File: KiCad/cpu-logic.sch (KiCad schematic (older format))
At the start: 27 parts, among them J1 Barrel_Jack, U1 LM555, U2 74LS05, U3 68000D, X1 CXO_DIP14

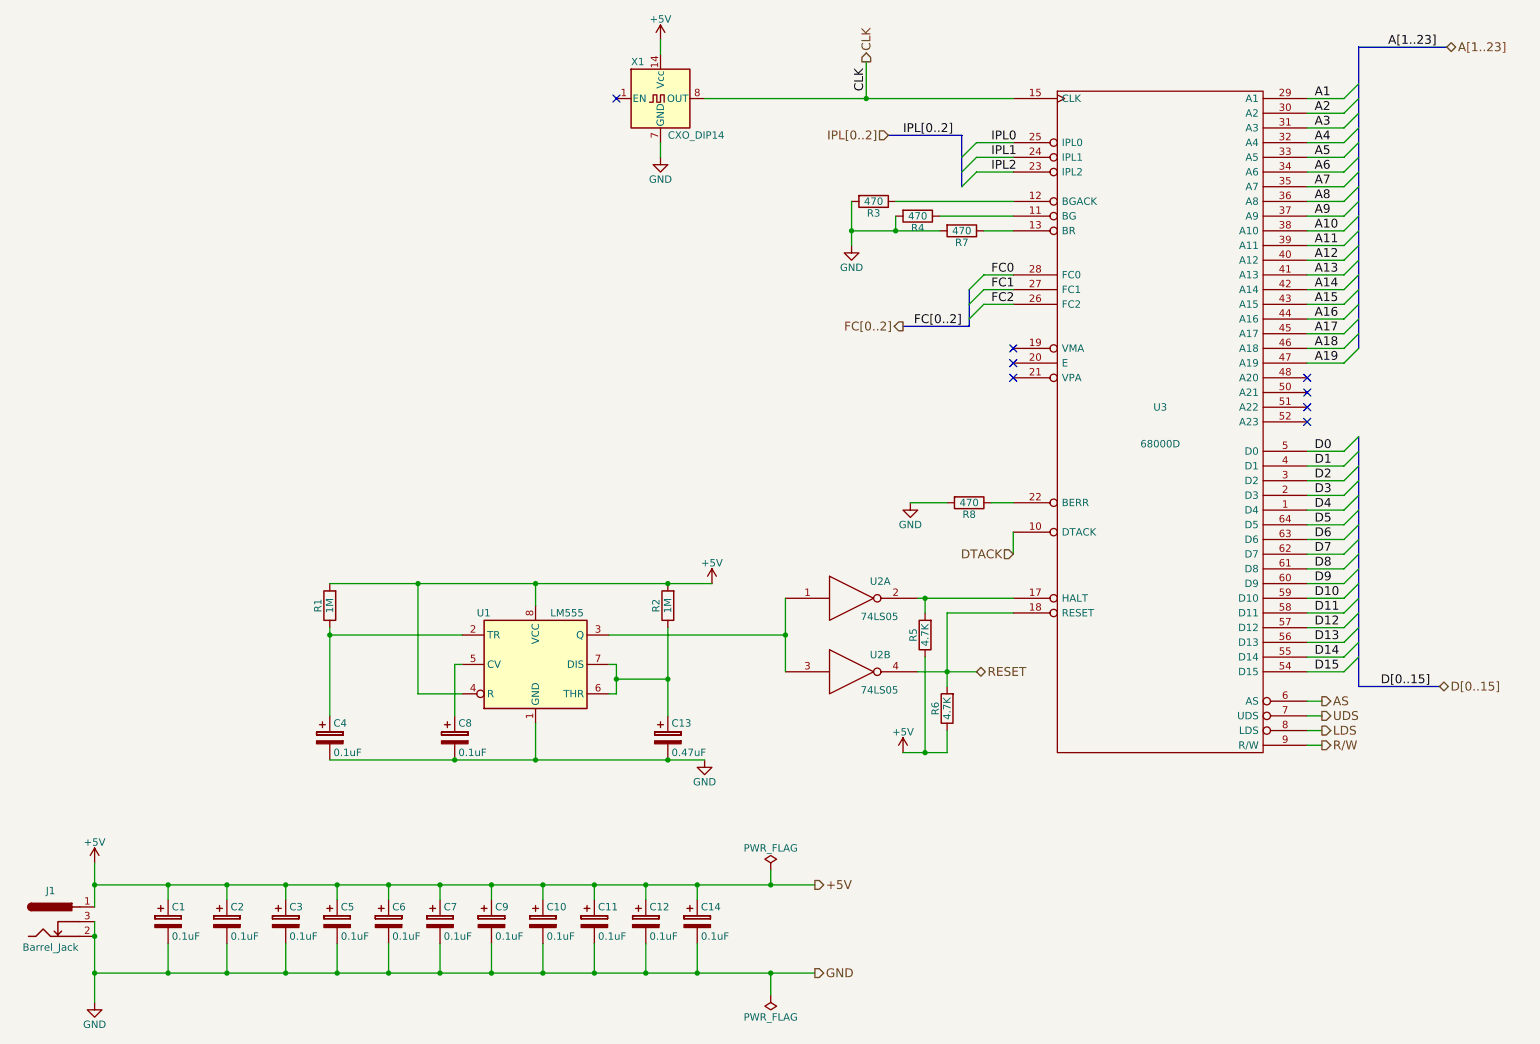
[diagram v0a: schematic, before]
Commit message: begin update for schematic
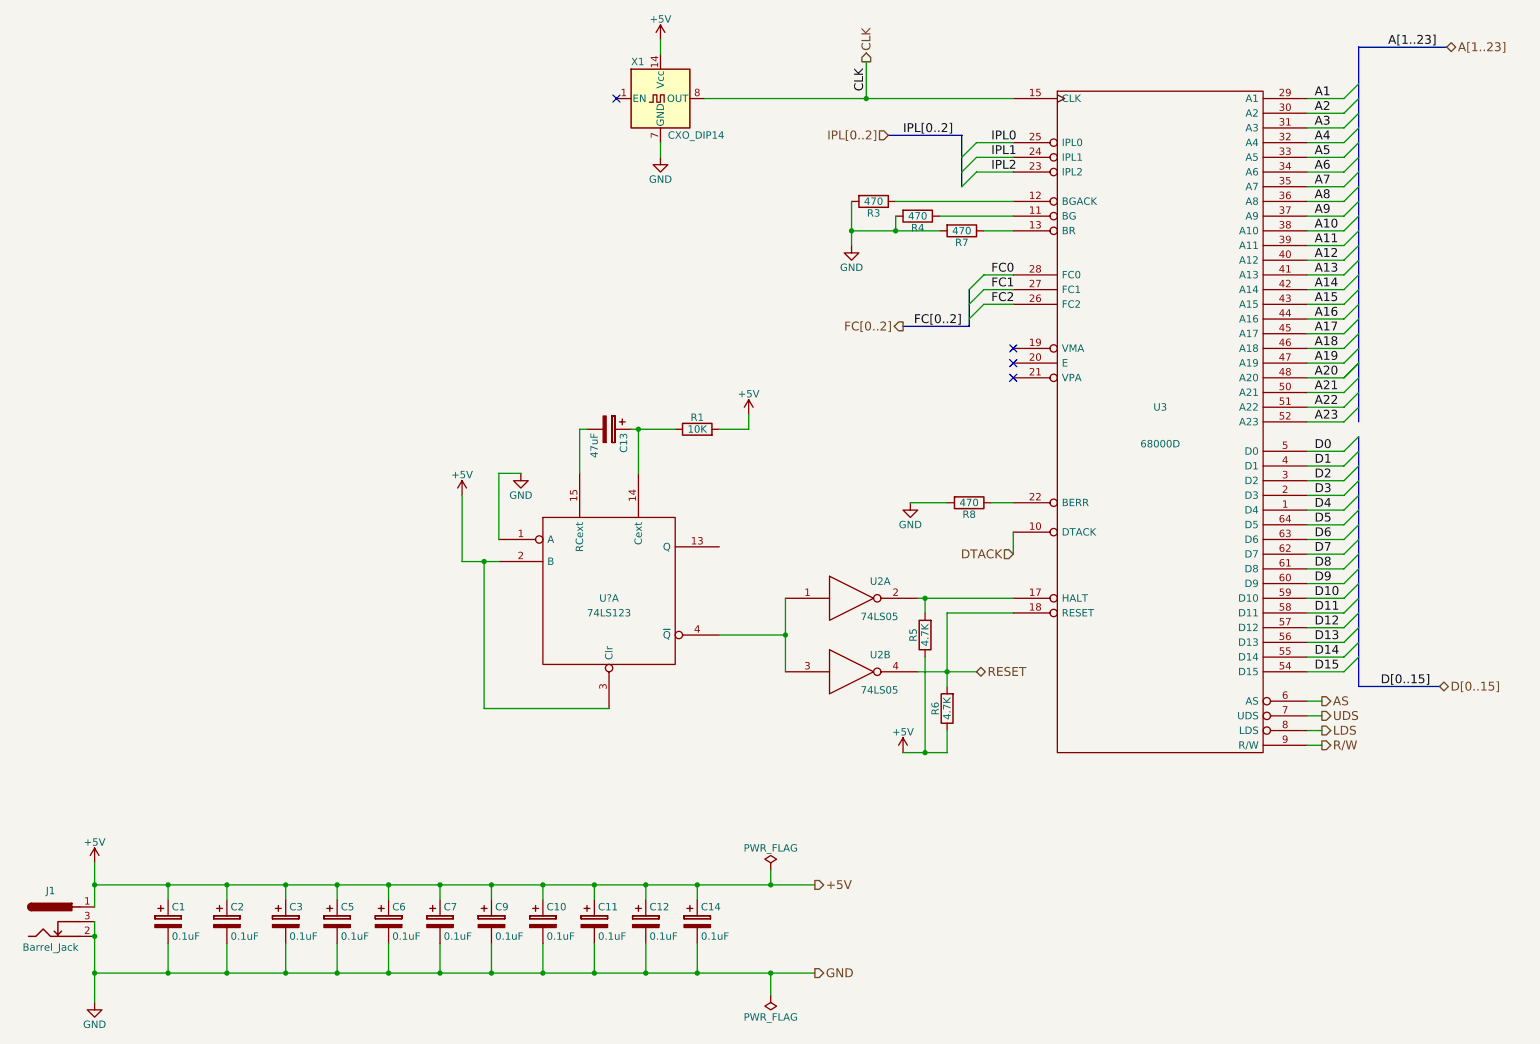
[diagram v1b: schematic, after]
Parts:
- removed C4, C8: 0.1uF, symbol CP
- removed R2: 1M, symbol R
- removed U1: LM555, symbol LM555
- added U?: 74LS123, symbol 74LS123
- C13: value 0.47uF -> 47uF
- R1: value 1M -> 10K
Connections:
- net +5V: now also U?.2 (B), U?.3 (Clr)
- net GND: now also U?.1 (A), U?.8 (GND); no longer C13.2
- net VCC: now also U?.16 (VCC)
- net A20: now reaches U3.48 (A20)
- net A21: now reaches U3.50 (A21)
- net A22: now reaches U3.51 (A22)
- net A23: now reaches U3.52 (A23)
- net at R1.1: now also C13.1, U?.14 (Cext)
- net at U2.1, U2.3: now also U?.4 (~Q)
- new net: C13.2, U?.15 (RCext)
- no-connect marks 8 -> 4
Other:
- moved on the sheet: C13, R1
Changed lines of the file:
@@
 EESchema Schematic File Version 2
 LIBS:Memory_RAM
-LIBS:Oscillator
 LIBS:power
 LIBS:device
@@
 LIBS:valves
 LIBS:Logic_74xx
-LIBS:xc9572xl
-LIBS:Timer_RTC
 LIBS:ds1501y
 LIBS:cp2102
@@
 $EndComp
 $Comp
-L LM555 U1
-U 1 1 5A62B1D1
-P 4250 5250
-F 0 "U1" H 3850 5600 50  0000 L CNN
-F 1 "LM555" H 4350 5600 50  0000 L CNN
-F 2 "" H 4250 5250 50  0001 C CNN
-F 3 "" H 4250 5250 50  0001 C CNN
-	1    4250 5250
-	1    0    0    -1
-$EndComp
-$Comp
 L 74LS05 U2
 U 1 1 5A62B26D
@@
 L +5V #PWR06
 U 1 1 5A62F126
-P 5450 4700
-F 0 "#PWR06" H 5450 4550 50  0001 C CNN
-F 1 "+5V" H 5450 4840 50  0000 C CNN
-F 2 "" H 5450 4700 50  0001 C CNN
-F 3 "" H 5450 4700 50  0001 C CNN
-	1    5450 4700
-	1    0    0    -1
-$EndComp
-$Comp
-L GND #PWR07
-U 1 1 5A62F228
-P 5400 5900
-F 0 "#PWR07" H 5400 5650 50  0001 C CNN
-F 1 "GND" H 5400 5750 50  0000 C CNN
-F 2 "" H 5400 5900 50  0001 C CNN
-F 3 "" H 5400 5900 50  0001 C CNN
-	1    5400 5900
+P 5700 3550
+F 0 "#PWR06" H 5700 3400 50  0001 C CNN
+F 1 "+5V" H 5700 3690 50  0000 C CNN
+F 2 "" H 5700 3550 50  0001 C CNN
+F 3 "" H 5700 3550 50  0001 C CNN
+	1    5700 3550
 	1    0    0    -1
 $EndComp
@@
 L R R1
 U 1 1 5A62F46A
-P 2850 4850
-F 0 "R1" V 2930 4850 50  0000 C CNN
-F 1 "1M" V 2850 4850 50  0000 C CNN
-F 2 "" V 2780 4850 50  0001 C CNN
-F 3 "" H 2850 4850 50  0001 C CNN
-	1    2850 4850
-	-1   0    0    1
-$EndComp
-$Comp
-L CP C8
-U 1 1 5A62F7CA
-P 3700 5750
-F 0 "C8" H 3725 5850 50  0000 L CNN
-F 1 "0.1uF" H 3725 5650 50  0000 L CNN
-F 2 "" H 3738 5600 50  0001 C CNN
-F 3 "" H 3700 5750 50  0001 C CNN
-	1    3700 5750
-	1    0    0    -1
-$EndComp
-$Comp
-L CP C4
-U 1 1 5A63C41B
-P 2850 5750
-F 0 "C4" H 2875 5850 50  0000 L CNN
-F 1 "0.1uF" H 2875 5650 50  0000 L CNN
-F 2 "" H 2888 5600 50  0001 C CNN
-F 3 "" H 2850 5750 50  0001 C CNN
-	1    2850 5750
-	1    0    0    -1
-$EndComp
-$Comp
-L R R2
-U 1 1 5A63C9D1
-P 5150 4850
-F 0 "R2" V 5230 4850 50  0000 C CNN
-F 1 "1M" V 5150 4850 50  0000 C CNN
-F 2 "" V 5080 4850 50  0001 C CNN
-F 3 "" H 5150 4850 50  0001 C CNN
-	1    5150 4850
-	-1   0    0    1
+P 5350 3650
+F 0 "R1" V 5430 3650 50  0000 C CNN
+F 1 "10K" V 5350 3650 50  0000 C CNN
+F 2 "" V 5280 3650 50  0001 C CNN
+F 3 "" H 5350 3650 50  0001 C CNN
+	1    5350 3650
+	0    -1   -1   0
 $EndComp
 $Comp
 L CP C13
 U 1 1 5A63CA8B
-P 5150 5750
-F 0 "C13" H 5175 5850 50  0000 L CNN
-F 1 "0.47uF" H 5175 5650 50  0000 L CNN
-F 2 "" H 5188 5600 50  0001 C CNN
-F 3 "" H 5150 5750 50  0001 C CNN
-	1    5150 5750
-	1    0    0    -1
+P 4750 3650
+F 0 "C13" H 4775 3750 50  0000 L CNN
+F 1 "47uF" H 4775 3550 50  0000 L CNN
+F 2 "" H 4788 3500 50  0001 C CNN
+F 3 "" H 4750 3650 50  0001 C CNN
+	1    4750 3650
+	0    1    1    0
 $EndComp
 $Comp
@@
 	5100 1700 5100 1800
 Wire Wire Line
-	4250 4700 4250 4850
-Wire Wire Line
-	2850 4700 5450 4700
-Wire Wire Line
 	6800 4150 7050 4150
-Connection ~ 4250 4700
-Wire Wire Line
-	3750 5450 3450 5450
-Wire Wire Line
-	3450 5450 3450 4700
-Wire Wire Line
-	4250 5900 4250 5650
-Wire Wire Line
-	2850 5900 5400 5900
-Connection ~ 4250 5900
-Wire Wire Line
-	3700 5600 3700 5250
-Wire Wire Line
-	3700 5250 3750 5250
-Wire Wire Line
-	3750 5050 2850 5050
-Wire Wire Line
-	2850 5000 2850 5600
-Connection ~ 2850 5050
-Connection ~ 3700 5900
-Connection ~ 3450 4700
-Wire Wire Line
-	4750 5250 4800 5250
-Wire Wire Line
-	4800 5250 4800 5450
-Wire Wire Line
-	4800 5450 4750 5450
-Connection ~ 5150 4700
-Wire Wire Line
-	4800 5350 5150 5350
-Wire Wire Line
-	5150 5000 5150 5600
-Connection ~ 4800 5350
-Connection ~ 5150 5350
-Connection ~ 5150 5900
-Wire Wire Line
-	4750 5050 5950 5050
 Wire Wire Line
 	5950 4800 5950 5300
-Connection ~ 5950 5050
 Wire Wire Line
 	6900 5200 6900 5850
@@
 	5350 6850 5350 6750
 Connection ~ 5350 6750
-NoConn ~ 9500 3300
-NoConn ~ 9500 3400
-NoConn ~ 9500 3500
-NoConn ~ 9500 3600
 Wire Bus Line
-	9850 1050 9850 3100
+	9850 1050 9850 3600
+$Comp
+L 74LS123 U?
+U 1 1 5B522F26
+P 4750 4750
+F 0 "U?" H 4750 4700 50  0000 C CNN
+F 1 "74LS123" H 4750 4600 50  0000 C CNN
+F 2 "" H 4750 4750 50  0001 C CNN
+F 3 "" H 4750 4750 50  0001 C CNN
+	1    4750 4750
+	1    0    0    -1
+$EndComp
+Wire Wire Line
+	4550 3950 4550 3650
+Wire Wire Line
+	4550 3650 4600 3650
+Wire Wire Line
+	4950 3950 4950 3650
+Wire Wire Line
+	4900 3650 5200 3650
+Connection ~ 4950 3650
+Wire Wire Line
+	5500 3650 5700 3650
+Wire Wire Line
+	5700 3650 5700 3550
+$Comp
+L GND #PWR?
+U 1 1 5B524750
+P 4150 3950
+F 0 "#PWR?" H 4150 3700 50  0001 C CNN
+F 1 "GND" H 4150 3800 50  0000 C CNN
+F 2 "" H 4150 3950 50  0001 C CNN
+F 3 "" H 4150 3950 50  0001 C CNN
+	1    4150 3950
+	1    0    0    -1
+$EndComp
+$Comp
+L +5V #PWR?
+U 1 1 5B5247BB
+P 3750 4100
+F 0 "#PWR?" H 3750 3950 50  0001 C CNN
+F 1 "+5V" H 3750 4240 50  0000 C CNN
+F 2 "" H 3750 4100 50  0001 C CNN
+F 3 "" H 3750 4100 50  0001 C CNN
+	1    3750 4100
+	1    0    0    -1
+$EndComp
+Wire Wire Line
+	4000 4550 3750 4550
+Wire Wire Line
+	3750 4550 3750 4100
+Wire Wire Line
+	4150 3950 4000 3950
+Wire Wire Line
+	4000 3950 4000 4400
+Wire Wire Line
+	4750 5550 3900 5550
+Wire Wire Line
+	3900 5550 3900 4550
+Connection ~ 3900 4550
+Wire Wire Line
+	5500 5050 5950 5050
+Connection ~ 5950 5050
+Wire Wire Line
+	9500 3300 9750 3300
+Wire Wire Line
+	9500 3400 9750 3400
+Wire Wire Line
+	9500 3500 9750 3500
+Wire Wire Line
+	9500 3600 9750 3600
+Text Label 9550 3300 0    60   ~ 0
+A20
+Text Label 9550 3400 0    60   ~ 0
+A21
+Text Label 9550 3500 0    60   ~ 0
+A22
+Text Label 9550 3600 0    60   ~ 0
+A23
+Entry Wire Line
+	9750 3300 9850 3200
+Entry Wire Line
+	9750 3300 9850 3200
+Entry Wire Line
+	9750 3400 9850 3300
+Entry Wire Line
+	9750 3500 9850 3400
+Entry Wire Line
+	9750 3600 9850 3500
 $EndSCHEMATC
